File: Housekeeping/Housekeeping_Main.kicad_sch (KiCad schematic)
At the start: 0 parts

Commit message: Added MCUs and pheriperal circuits
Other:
- added sheet MCU (MCUsch.kicad_sch)
- added sheet Power_Architecture (Power_arch.kicad_sch)
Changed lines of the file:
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@@
 	(generator_version "10.0")
 	(paper "A4")
+	(sheet
+		(at 16.51 18.415)
+		(size 61.595 24.13)
+		(exclude_from_sim no)
+		(in_bom yes)
+		(on_board yes)
+		(dnp no)
+		(fields_autoplaced yes)
+		(stroke
+			(width 0.1524)
+			(type solid)
+		)
+		(fill
+			(color 0 0 0 0)
+		)
+		(property "Sheetname" "MCU"
+			(at 16.51 17.7034 0)
+			(show_name no)
+			(do_not_autoplace no)
+			(effects
+				(font
+					(size 1.27 1.27)
+				)
+				(justify left bottom)
+			)
+		)
+		(property "Sheetfile" "MCUsch.kicad_sch"
+			(at 16.51 43.1296 0)
+			(show_name no)
+			(do_not_autoplace no)
+			(effects
+				(font
+					(size 1.27 1.27)
+				)
+				(justify left top)
+			)
+		)
+		(instances
+			(project "Housekeeping_Main"
+				(path "/ab76f670-e2c0-47ab-9a32-a91d60c28fa5"
+					(page "2")
+				)
+			)
+		)
+	)
+	(sheet
+		(at 17.145 55.245)
+		(size 62.23 25.4)
+		(exclude_from_sim no)
+		(in_bom yes)
+		(on_board yes)
+		(dnp no)
+		(fields_autoplaced yes)
+		(stroke
+			(width 0.1524)
+			(type solid)
+		)
+		(fill
+			(color 0 0 0 0)
+		)
+		(property "Sheetname" "Power_Architecture"
+			(at 17.145 54.5334 0)
+			(show_name no)
+			(do_not_autoplace no)
+			(effects
+				(font
+					(size 1.27 1.27)
+				)
+				(justify left bottom)
+			)
+		)
+		(property "Sheetfile" "Power_arch.kicad_sch"
+			(at 17.145 81.2296 0)
+			(show_name no)
+			(do_not_autoplace no)
+			(effects
+				(font
+					(size 1.27 1.27)
+				)
+				(justify left top)
+			)
+		)
+		(instances
+			(project "Housekeeping_Main"
+				(path "/ab76f670-e2c0-47ab-9a32-a91d60c28fa5"
+					(page "3")
+				)
+			)
+		)
+	)
 	(sheet_instances
 		(path "/"

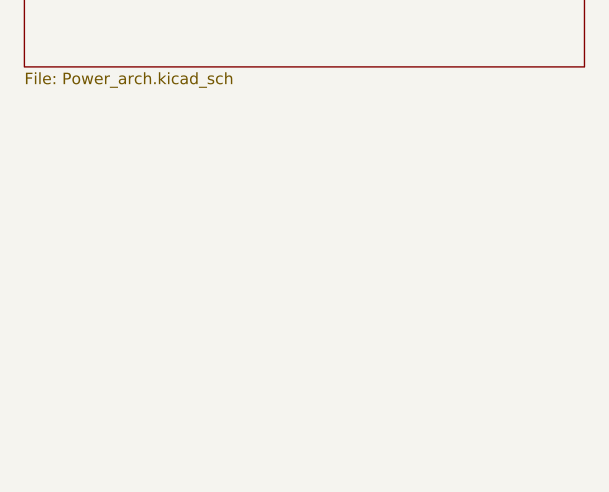
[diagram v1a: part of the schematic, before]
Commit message: Implemented CAN
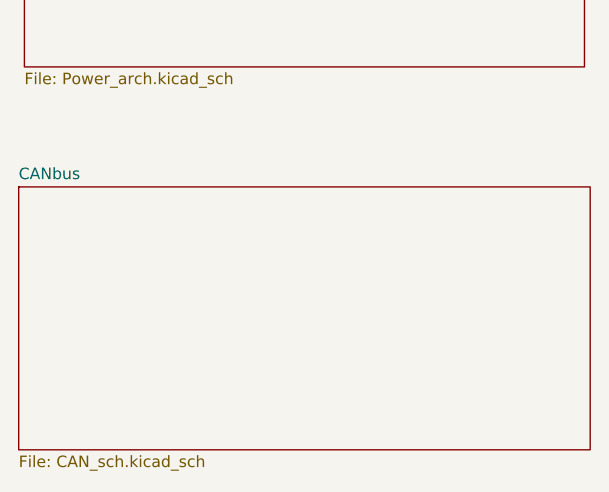
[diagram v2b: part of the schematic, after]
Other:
- added sheet CANbus (CAN_sch.kicad_sch)
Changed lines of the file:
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@@
+		)
+	)
+	(sheet
+		(at 16.51 93.98)
+		(size 63.5 29.21)
+		(exclude_from_sim no)
+		(in_bom yes)
+		(on_board yes)
+		(dnp no)
+		(fields_autoplaced yes)
+		(stroke
+			(width 0.1524)
+			(type solid)
+		)
+		(fill
+			(color 0 0 0 0)
+		)
+		(property "Sheetname" "CANbus"
+			(at 16.51 93.2684 0)
+			(show_name no)
+			(do_not_autoplace no)
+			(effects
+				(font
+					(size 1.27 1.27)
+				)
+				(justify left bottom)
+			)
+		)
+		(property "Sheetfile" "CAN_sch.kicad_sch"
+			(at 16.51 123.7746 0)
+			(show_name no)
+			(do_not_autoplace no)
+			(effects
+				(font
+					(size 1.27 1.27)
+				)
+				(justify left top)
+			)
+		)
+		(instances
+			(project "Housekeeping_Main"
+				(path "/ab76f670-e2c0-47ab-9a32-a91d60c28fa5"
+					(page "4")
+				)
+			)
 		)
 	)

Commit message: added page titles to schematics
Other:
- company: (none) -> Team Anant - Guru Tanish
- title: (none) -> Housekeeping Board
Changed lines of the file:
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@@
 	(generator_version "10.0")
 	(paper "A4")
+	(title_block
+		(title "Housekeeping Board")
+		(company "Team Anant - Guru Tanish")
+	)
 	(sheet
 		(at 16.51 18.415)

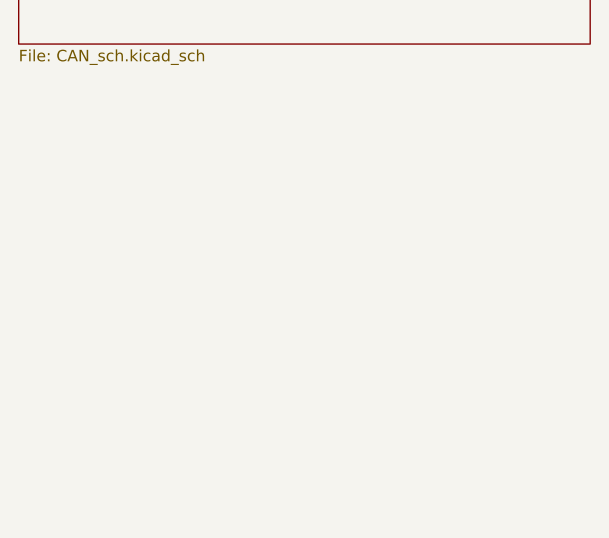
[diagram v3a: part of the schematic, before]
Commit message: added LTC 2986 module
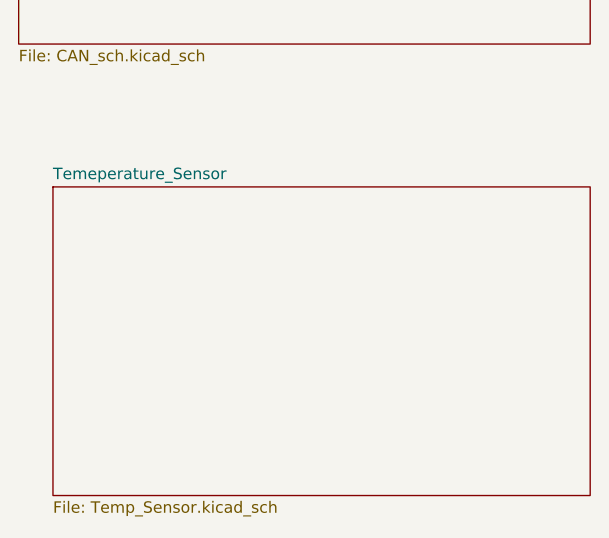
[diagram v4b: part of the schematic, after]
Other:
- added sheet Temeperature_Sensor (Temp_Sensor.kicad_sch)
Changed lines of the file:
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@@
+	)
+	(sheet
+		(at 20.32 139.065)
+		(size 59.69 34.29)
+		(exclude_from_sim no)
+		(in_bom yes)
+		(on_board yes)
+		(dnp no)
+		(fields_autoplaced yes)
+		(stroke
+			(width 0.1524)
+			(type solid)
+		)
+		(fill
+			(color 0 0 0 0)
+		)
+		(property "Sheetname" "Temeperature_Sensor"
+			(at 20.32 138.3534 0)
+			(show_name no)
+			(do_not_autoplace no)
+			(effects
+				(font
+					(size 1.27 1.27)
+				)
+				(justify left bottom)
+			)
+		)
+		(property "Sheetfile" "Temp_Sensor.kicad_sch"
+			(at 20.32 173.9396 0)
+			(show_name no)
+			(do_not_autoplace no)
+			(effects
+				(font
+					(size 1.27 1.27)
+				)
+				(justify left top)
+			)
+		)
+		(instances
+			(project "Housekeeping_Main"
+				(path "/ab76f670-e2c0-47ab-9a32-a91d60c28fa5"
+					(page "5")
+				)
+			)
+		)
 	)
 	(sheet

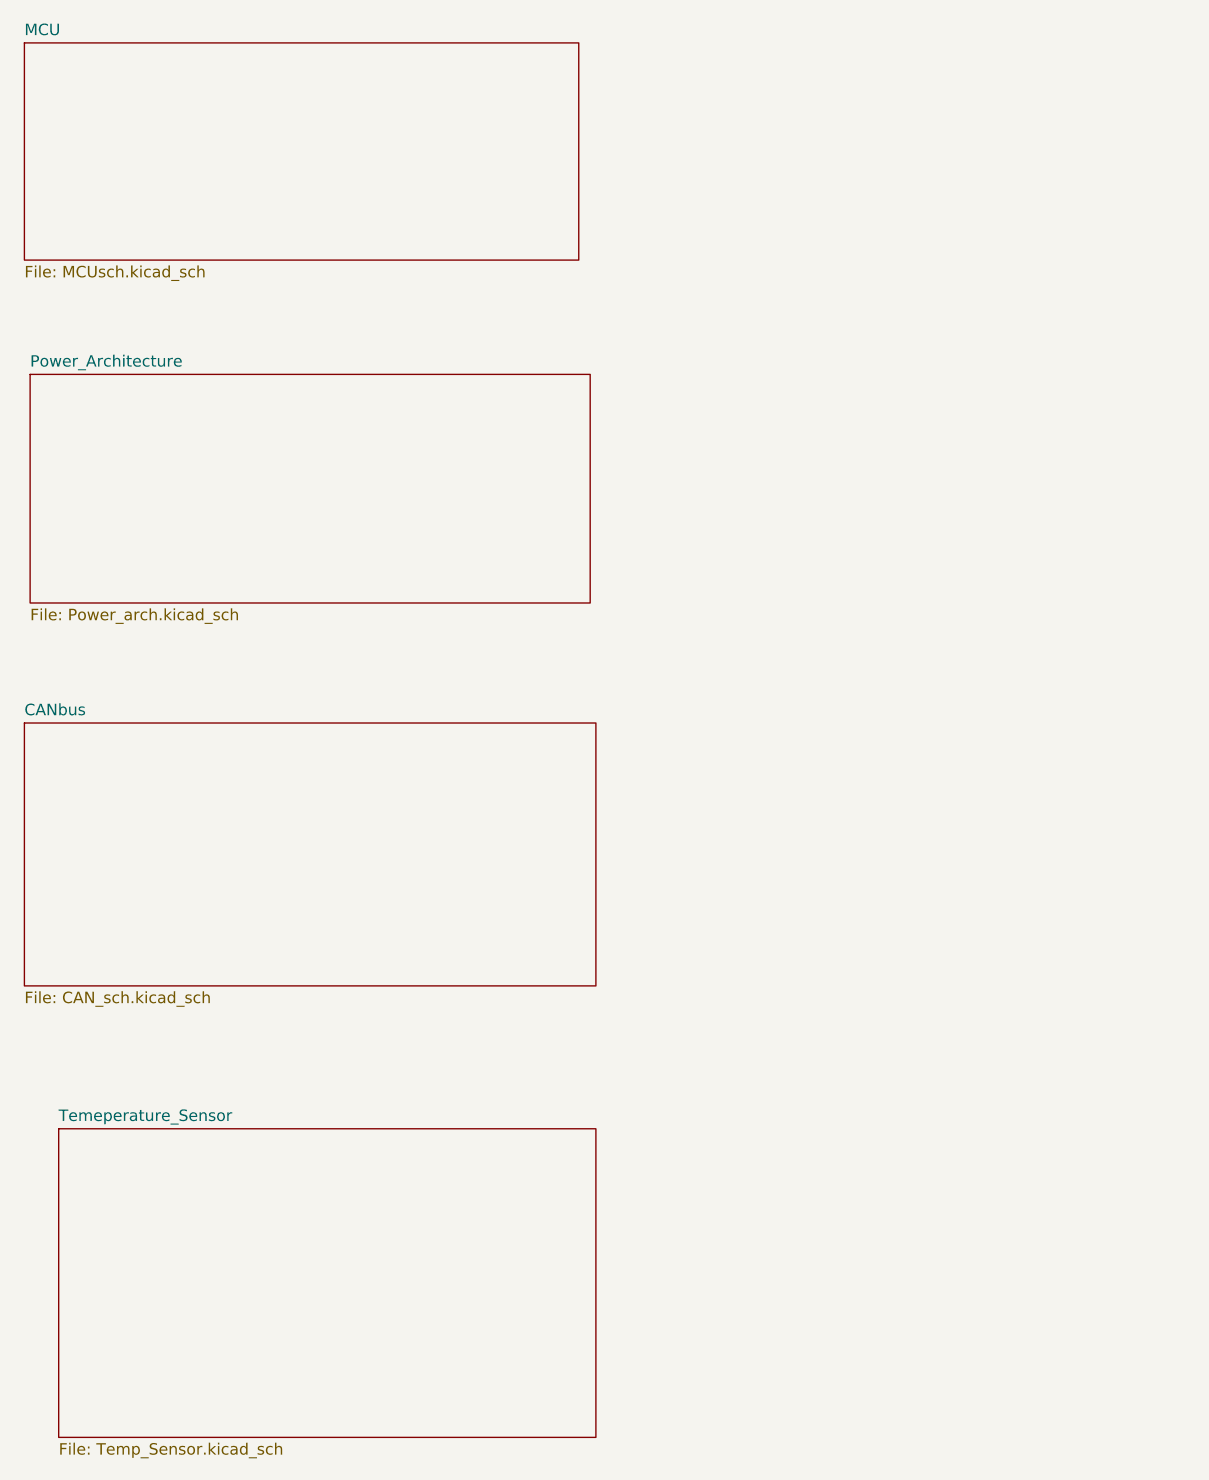
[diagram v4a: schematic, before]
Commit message: Added PC104 Cubesat Standard
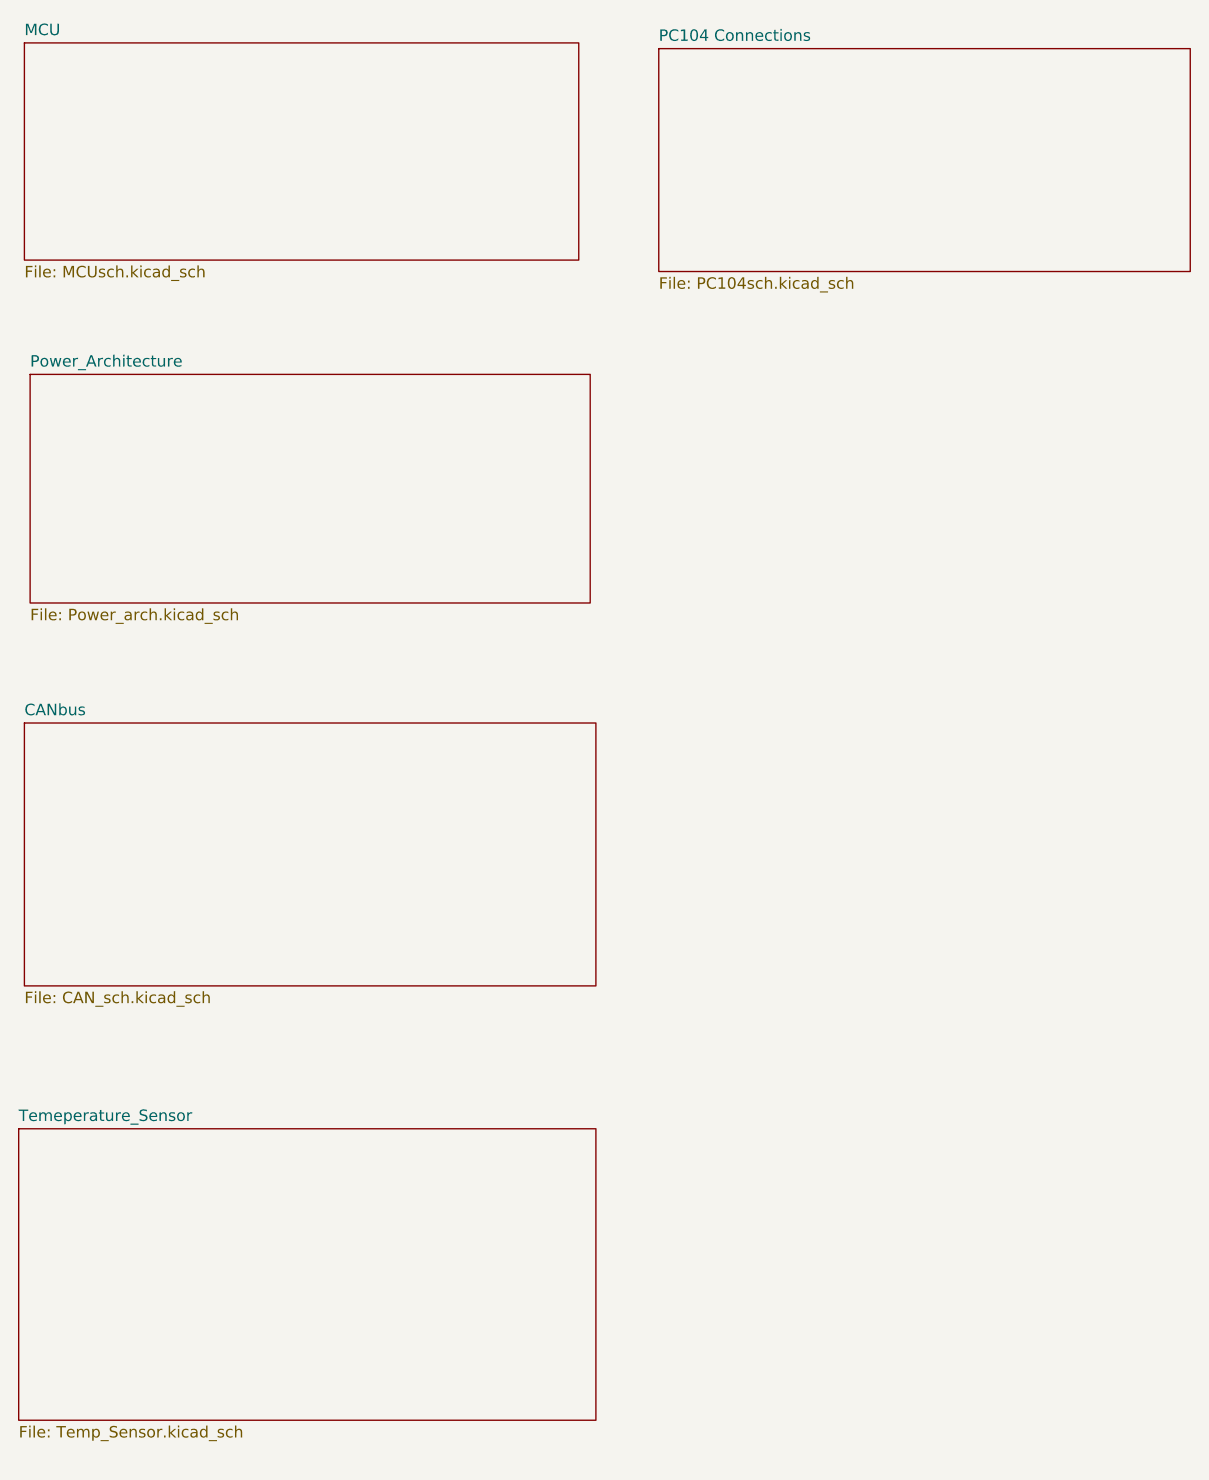
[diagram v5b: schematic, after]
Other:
- added sheet PC104 Connections (PC104sch.kicad_sch)
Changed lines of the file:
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@@
 	)
 	(sheet
-		(at 20.32 139.065)
-		(size 59.69 34.29)
+		(at 15.875 139.065)
+		(size 64.135 32.385)
 		(exclude_from_sim no)
 		(in_bom yes)
@@
 		)
 		(property "Sheetname" "Temeperature_Sensor"
-			(at 20.32 138.3534 0)
+			(at 15.875 138.3534 0)
 			(show_name no)
 			(do_not_autoplace no)
@@
 		)
 		(property "Sheetfile" "Temp_Sensor.kicad_sch"
-			(at 20.32 173.9396 0)
+			(at 15.875 172.0346 0)
 			(show_name no)
 			(do_not_autoplace no)
@@
 				)
 			)
+		)
+	)
+	(sheet
+		(at 86.995 19.05)
+		(size 59.055 24.765)
+		(exclude_from_sim no)
+		(in_bom yes)
+		(on_board yes)
+		(dnp no)
+		(fields_autoplaced yes)
+		(stroke
+			(width 0.1524)
+			(type solid)
+		)
+		(fill
+			(color 0 0 0 0)
+		)
+		(property "Sheetname" "PC104 Connections"
+			(at 86.995 18.3384 0)
+			(show_name no)
+			(do_not_autoplace no)
+			(effects
+				(font
+					(size 1.27 1.27)
+				)
+				(justify left bottom)
+			)
+		)
+		(property "Sheetfile" "PC104sch.kicad_sch"
+			(at 86.995 44.3996 0)
+			(show_name no)
+			(do_not_autoplace no)
+			(effects
+				(font
+					(size 1.27 1.27)
+				)
+				(justify left top)
+			)
+		)
+		(instances
+			(project "Housekeeping_Main"
+				(path "/ab76f670-e2c0-47ab-9a32-a91d60c28fa5"
+					(page "6")
+				)
+			)
